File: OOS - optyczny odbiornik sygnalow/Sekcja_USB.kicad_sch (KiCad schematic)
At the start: 1 part, among them J6 USB_C_Receptacle

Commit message: Finish Li-Lion section, add for review
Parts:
- added C23: 100n, Capacitor_SMD:C_0603_1608Metric_Pad1.08x0.95mm_HandSolder, symbol Device:C
- added C24: 4u7, Capacitor_SMD:C_0603_1608Metric, symbol Device:C
- added D7: SMAJ5.0A-TR, Diode_SMD:D_SMA_Handsoldering, symbol Diode:SMAJ5.0A
- added F1: 0ZCJ0110FF2E, Fuse:Fuse_1206_3216Metric, symbol Device:Fuse
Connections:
- net at J6.A4 (VBUS), J6.A9 (VBUS), J6.B4 (VBUS)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: now also F1.1
- new net: D7.1 (A1), F1.2
- new net 0V: D7.2 (A2)
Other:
- note added: "500mA fuse"

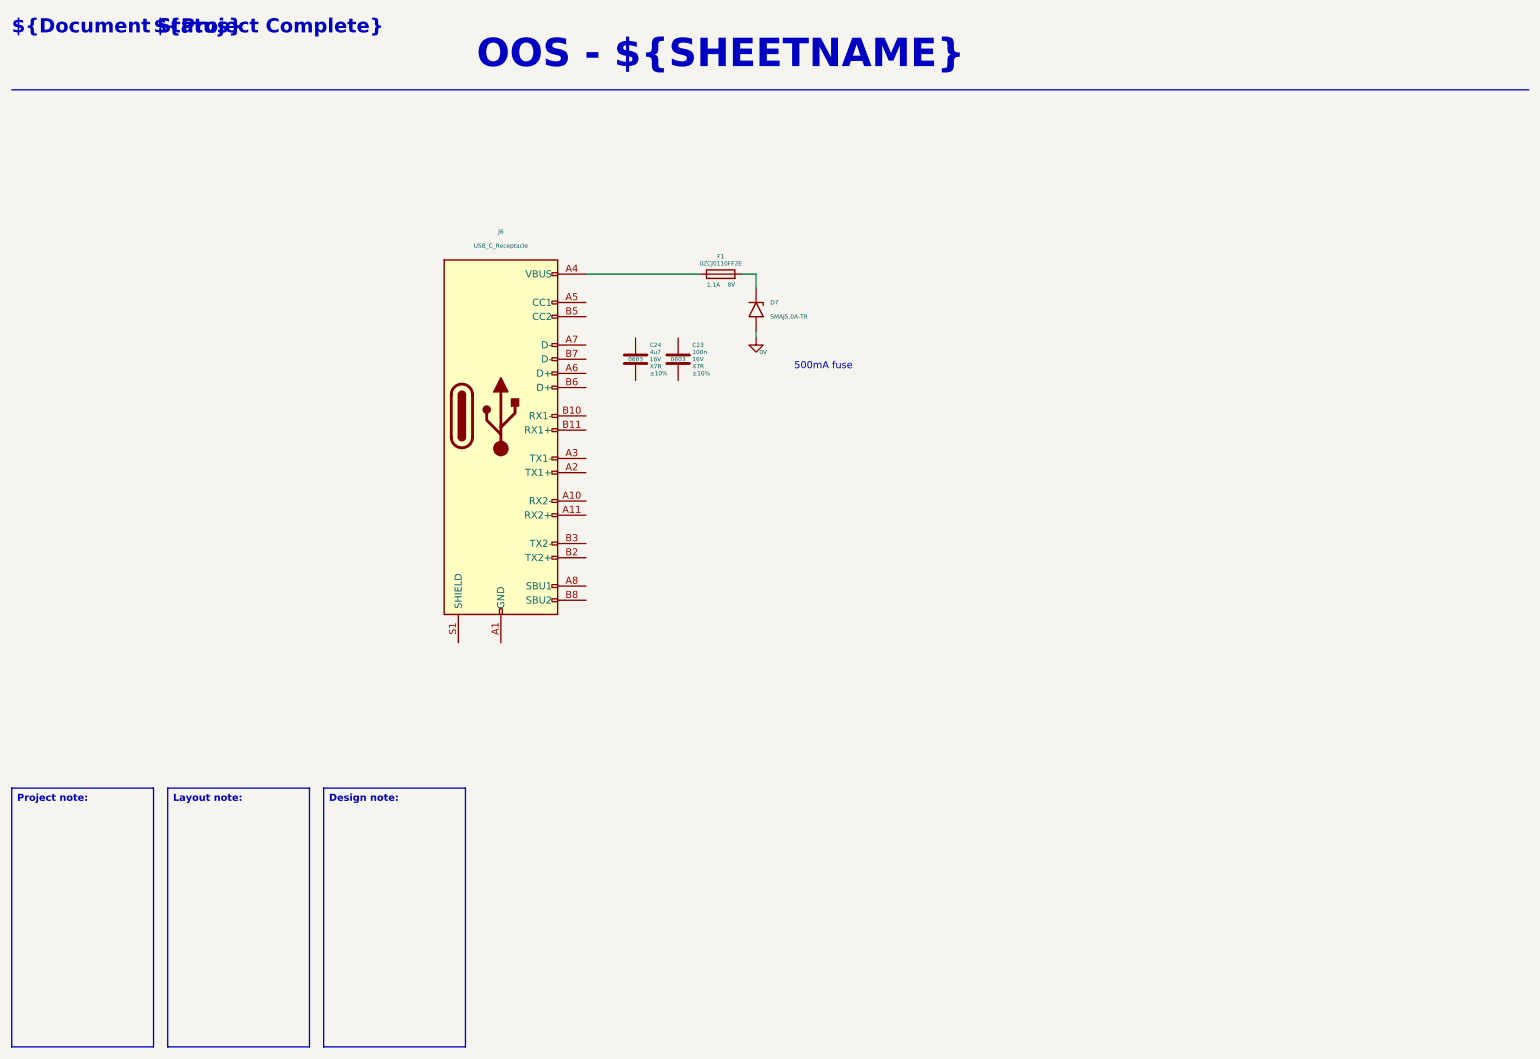
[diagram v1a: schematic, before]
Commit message: Implementing changes after review on Li-Ion section, adding components to USB section
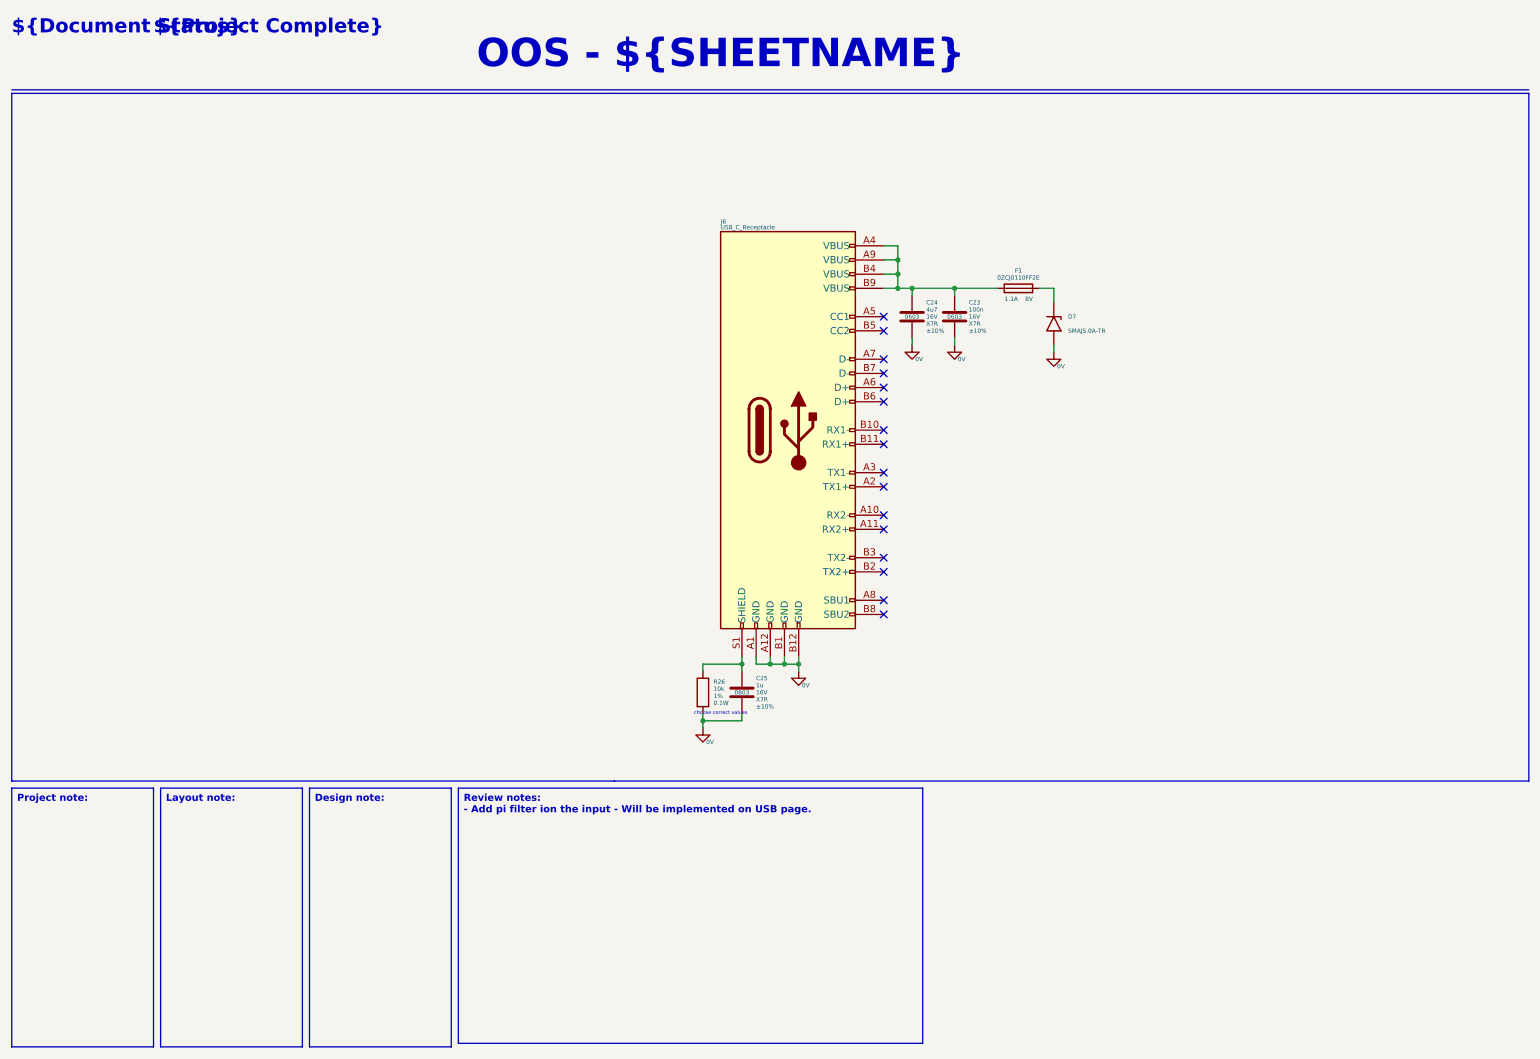
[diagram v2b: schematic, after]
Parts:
- added C25: 1u, Capacitor_SMD:C_0603_1608Metric_Pad1.08x0.95mm_HandSolder, symbol Device:C
- added R26: 10k, Resistor_SMD:R_0603_1608Metric, symbol Device:R
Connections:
- net 0V: now also C23.2, C24.2, J6.A1 (GND), J6.A12 (GND), J6.B1 (GND), J6.B12 (GND), C25.2, R26.2
- net at F1.1, J6.A4 (VBUS), J6.A9 (VBUS)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: now also C23.1, C24.1
- net at J6.S1 (SHIELD): now also C25.1, R26.1
- no-connect marks 0 -> 16
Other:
- note added: "choose correct values"
- note removed: "500mA fuse"
- moved on the sheet: C23, C24, D7, F1

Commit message: Adding Pi ferrite beat for PI filter on USB, changing RC values for SHIELD pin
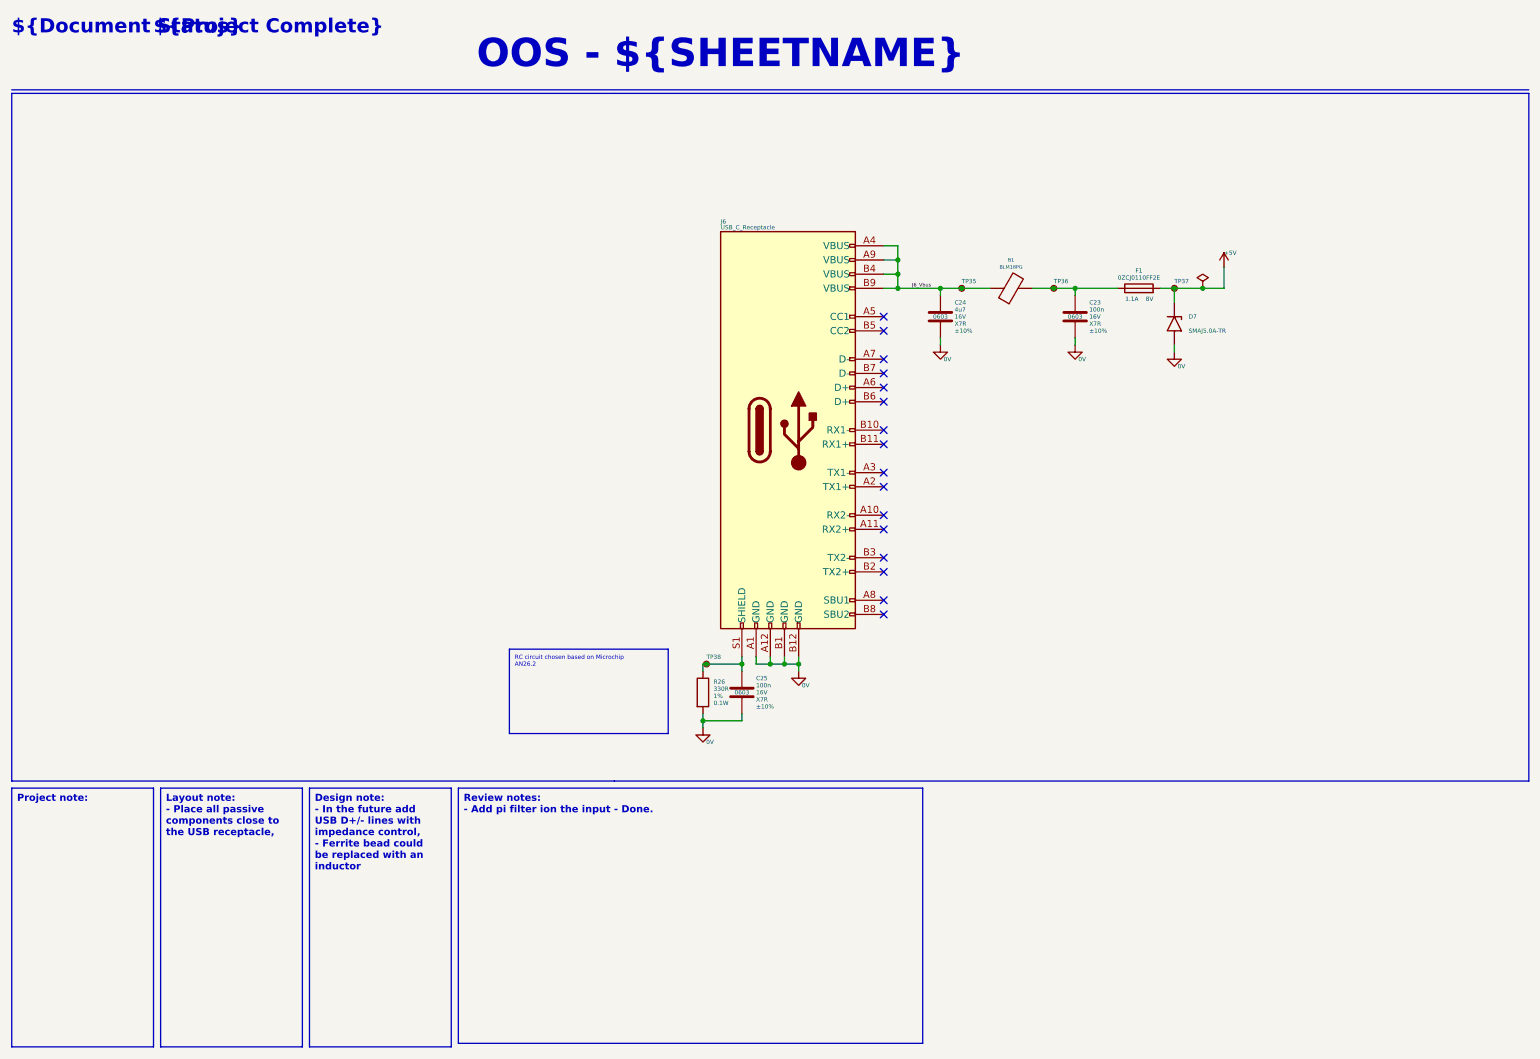
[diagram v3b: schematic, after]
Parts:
- added B1: BLM18PG, Inductor_SMD:L_0603_1608Metric, symbol Device:FerriteBead
- added TP35, TP36, TP37, TP38: TestPoint_Small, TestPoint:TestPoint_Pad_D1.0mm, symbol Connector:TestPoint_Small
- C25: value 1u -> 100n; MPN CC0603KRX7R7BB105 -> CL10B104KO8WPNC; Supplier Link https://www.tme.eu/pl/details/cc0603krx7r7bb105/kondensator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 -> https://www.tme.eu/pl/details/cl10b104ko8wpnc/kondensatory-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
- R26: value 10k -> 330R; Supplier Link https://www.tme.eu/pl/en/details/ac0603fr-0710kl/smd-resist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 -> https://www.tme.eu/pl/details/rc0603fr-07330r/rezystory-smd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; Temperature Coefficient 100 PPM/C -> 200 PPM/C; Voltage Rating 75 V -> 50V
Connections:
- net J6_Vbus: now reaches C24.1, J6.A4 (VBUS), J6.A9 (VBUS), J6.B4 (VBUS), J6.B9 (VBUS)
- net J6_Vbus: now also B1.1, TP35.1; no longer C23.1, F1.1
- net +5V: now reaches D7.1 (A1), F1.2
- net +5V: now also TP37.1
- net at C25.1, J6.S1 (SHIELD), R26.1: now also TP38.1
- new net: B1.2, C23.1, F1.1, TP36.1
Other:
- note removed: "choose correct values"
- moved on the sheet: C23, C24, D7, F1

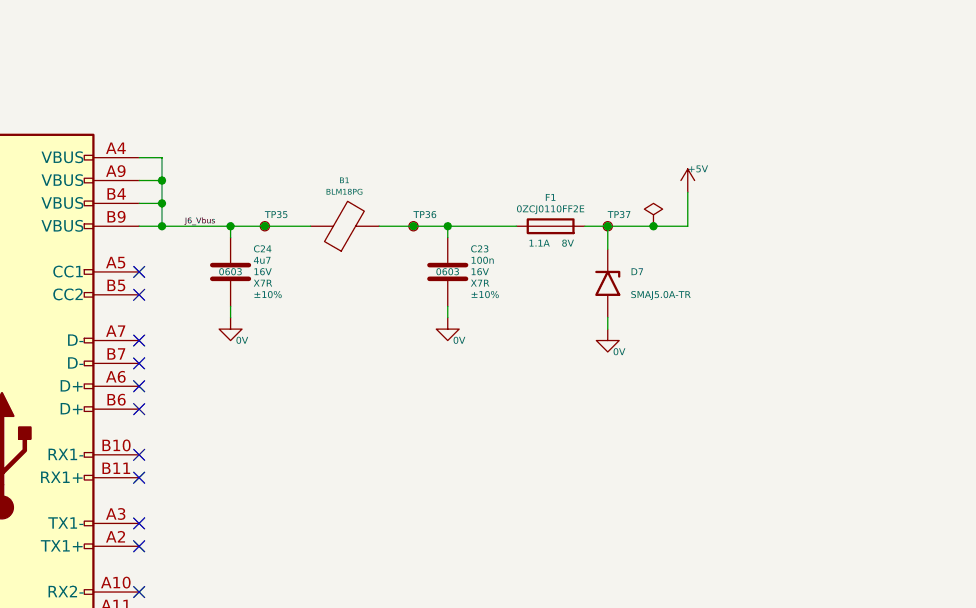
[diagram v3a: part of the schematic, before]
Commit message: Adding calciulations for PI filter, moving PI filter after the fuse, replacing ferrite bead with inductor
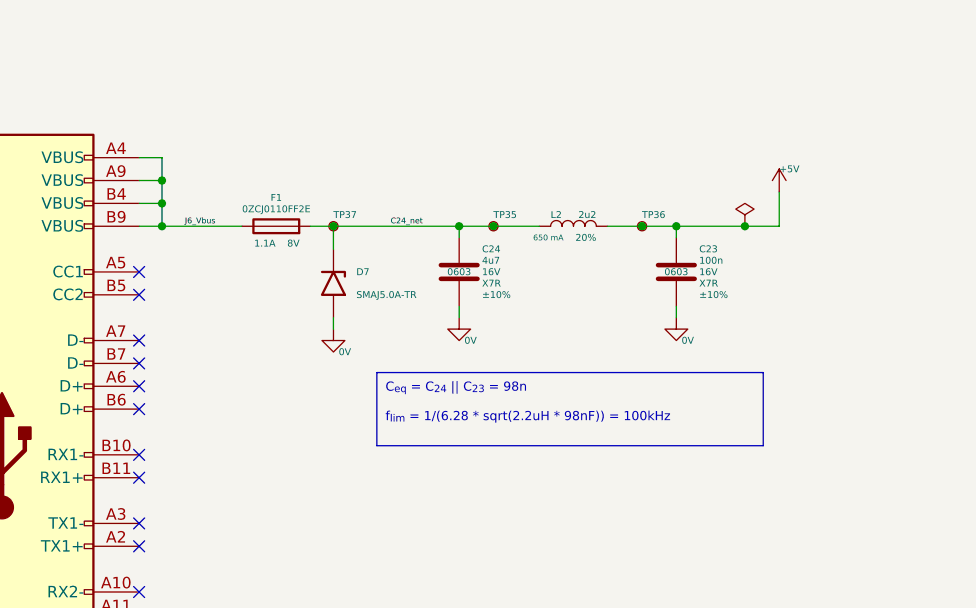
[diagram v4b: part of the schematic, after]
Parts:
- removed B1: BLM18PG, Inductor_SMD:L_0603_1608Metric, symbol Device:FerriteBead
- added L2: 2u2, Inductor_SMD:L_0805_2012Metric, symbol Device:L
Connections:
- net +5V: now also C23.1, TP36.1, L2.2; no longer D7.1 (A1), F1.2, TP37.1
- net J6_Vbus: now also F1.1; no longer C24.1, TP35.1
- new net C24_net: C24.1, D7.1 (A1), F1.2, L2.1, TP35.1, TP37.1
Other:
- moved on the sheet: C23, C24, D7, F1, TP35, TP36, TP37

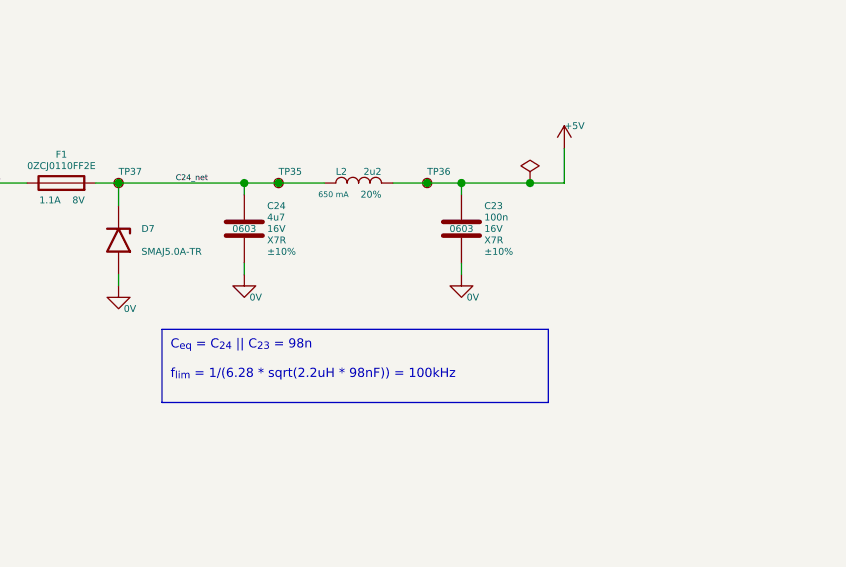
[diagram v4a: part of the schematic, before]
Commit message: Changing the inductor at USB Pi filter for higher current. Changing the capacitors as well so cutoff frequency is around 15 kHz
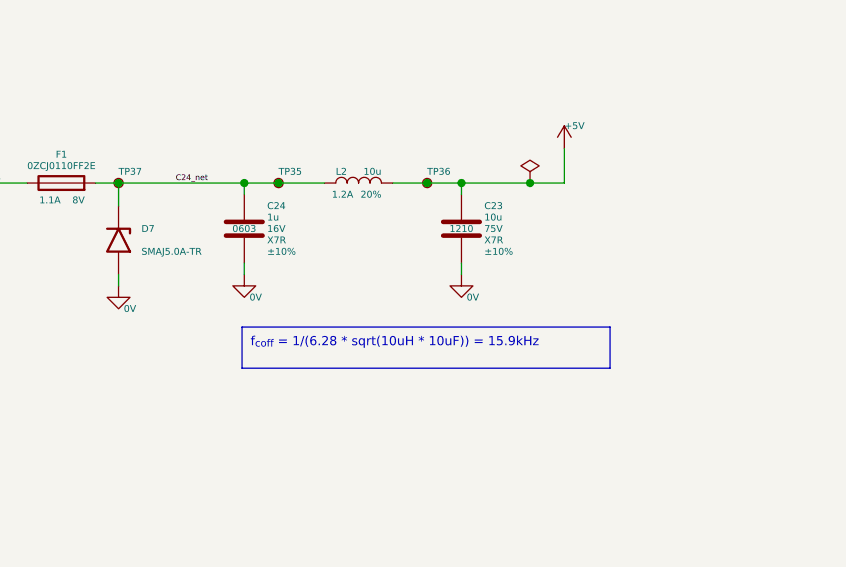
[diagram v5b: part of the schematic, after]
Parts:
- C23: value 100n -> 10u; footprint Capacitor_SMD:C_0603_1608Metric_Pad1.08x0.95mm_HandSolder -> Capacitor_SMD:C_1210_3225Metric_Pad1.33x2.70mm_HandSolder; MPN CL10B104KO8WPNC -> (none); Package 0603 -> 1210; Supplier Link https://www.tme.eu/pl/details/cl10b104ko8wpnc/kondensatory-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 -> https://www.tme.eu/pl/en/details/cga6p1x7r1n106kac/mlcc-smd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; Voltage Rating 16V -> 75V
- C24: value 4u7 -> 1u; footprint Capacitor_SMD:C_0603_1608Metric -> Capacitor_SMD:C_0603_1608Metric_Pad1.08x0.95mm_HandSolder; MPN (none) -> CC0603KRX7R7BB105; Supplier Link https://www.tme.eu/pl/en/details/grm188z71c475ke21d/mlcc-sm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 -> https://www.tme.eu/pl/details/cc0603krx7r7bb105/kondensator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
- L2: value 2u2 -> 10u; footprint Inductor_SMD:L_0805_2012Metric -> Inductor_SMD:L_Vishay_IHLP-1212; Max current (none) -> 1.2A; Max. Current 650 mA -> (none); Name MLZ2012A2R2WT000 -> LQH3NPN100MJRL; Package 0805 -> 1212; Supplier Link https://www.tme.eu/pl/details/mlz2012a2r2wt000/dlawiki/tdk/ -> (none); Supplier link (none) -> https://www.tme.eu/pl/details/lqh3npn100mjrl/dlawiki/murata/
